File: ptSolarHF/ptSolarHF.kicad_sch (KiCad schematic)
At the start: 55 parts, among them J1 6 Pin Male Header, J2 Programming, Q5 DMP2004K-7, U1 LP3985IM5-3.3/NOPB, U2 ATMega 328p-AU, U3 Si5351A-B-GT, U4 ATGM336H-5N31, U5 APX803S (SOT23SA), Y1 8MHz, Y2 27MHz Xtal - 7M-27.000MEEQ-T

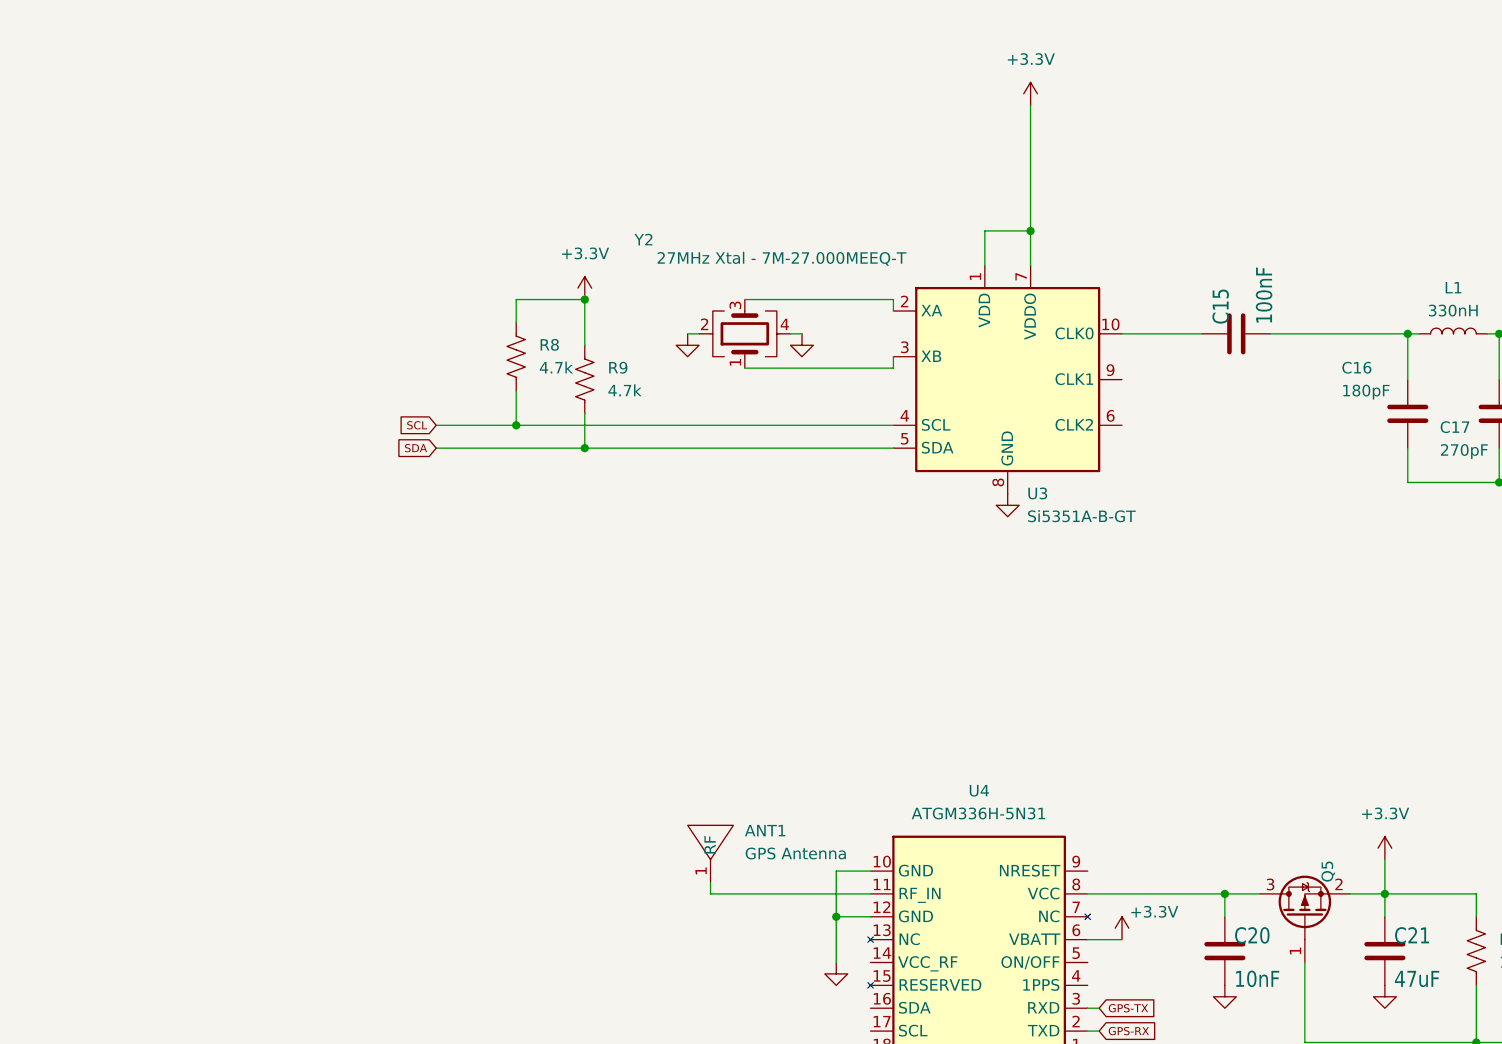
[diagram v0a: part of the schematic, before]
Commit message: 26MHz TCXO and version 2.0.0 of PCB
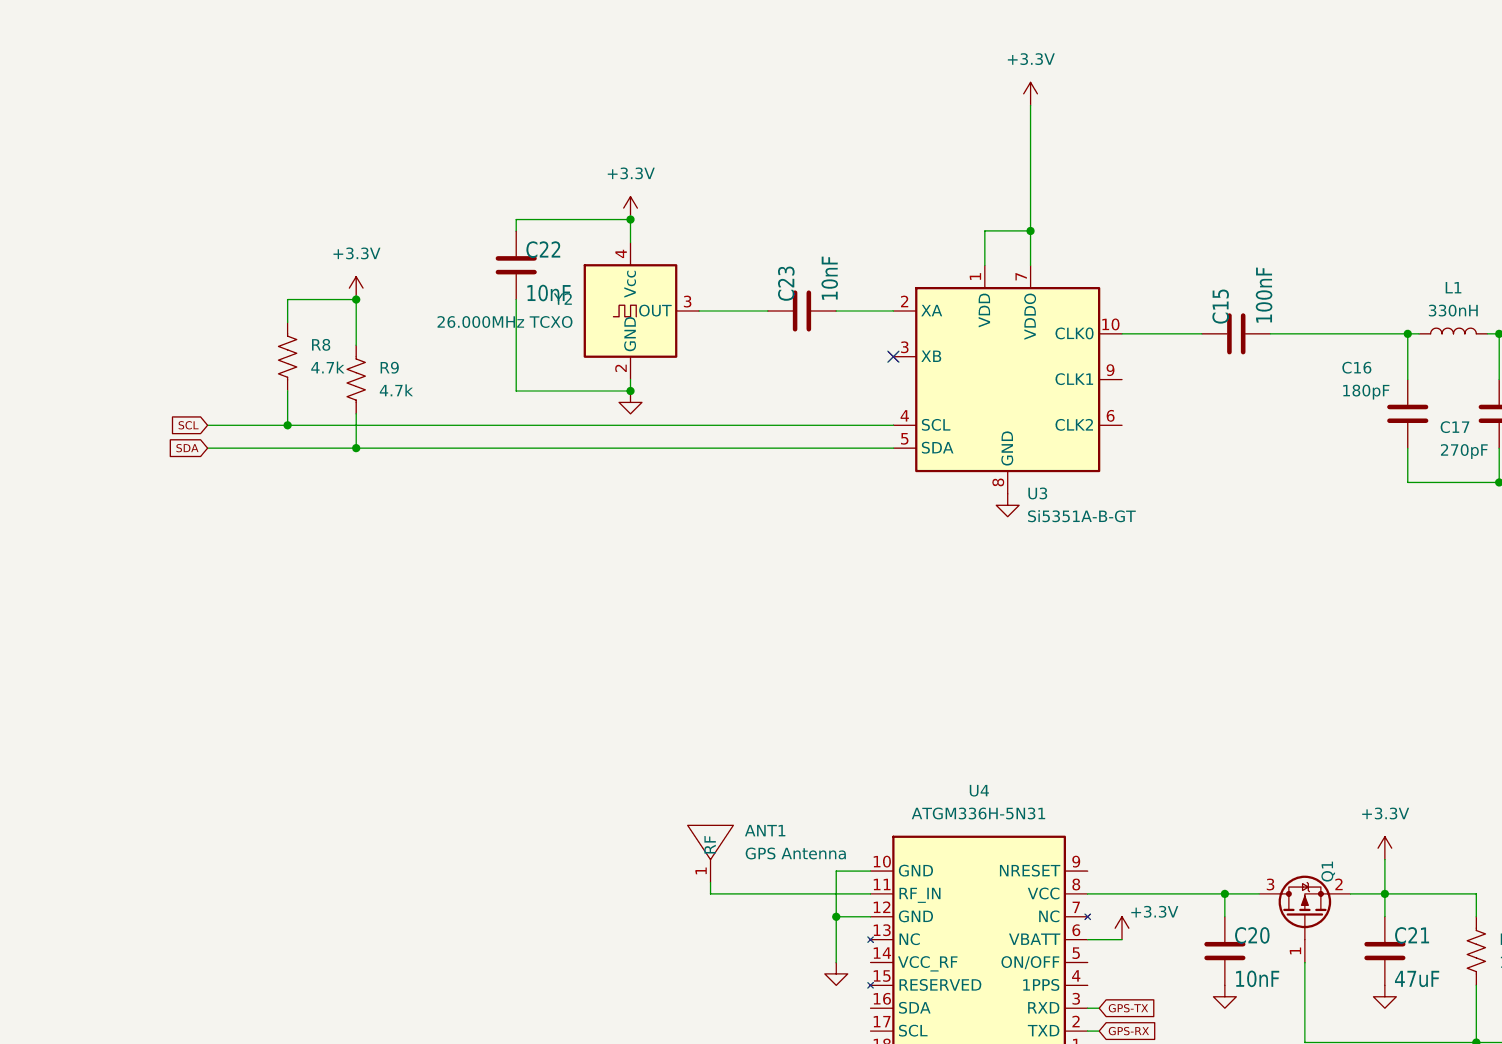
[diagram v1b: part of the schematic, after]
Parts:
- removed Y2: 27MHz Xtal - 7M-27.000MEEQ-T, Crystal:Crystal_SMD_3225-4Pin_3.2x2.5mm, symbol Device:Crystal_GND24
- added C22, C23: 10nF, Capacitor_SMD:C_0805_2012Metric, symbol Device:C
- added Y2: 26.000MHz TCXO, Oscillator:Oscillator_SMD_SeikoEpson_TG2520SMN-xxx-xxxxxx-4Pin_2.5x2.0mm, symbol Oscillator:TG2520SMN-xx.xxxxxxMhz-xxxxNM
- Q1: renamed from Q5; PosAdjust (none) -> 180
- U1, U5: PosAdjust (none) -> 180
- U2, U3, U4: PosAdjust (none) -> -90
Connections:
- net +3.3V: now also C22.1, Y2.4 (Vcc)
- net GND: now also C22.2, Y2.2 (GND)
- net at U3.2 (XA): now also C23.2
- new net: C23.1, Y2.3 (OUT)
- no-connect marks 0 -> 1
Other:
- moved on the sheet: R8, R9
